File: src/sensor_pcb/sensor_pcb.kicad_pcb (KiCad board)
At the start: 2 copper layers, 34 parts, among them IC1 TCAN3414DRBR, J1 662004231722, J2 643280100305, J3 66200821022, J4 66200821022, J5 662004231722, J6 643280100305, Q2 NPN BJT 40V 200mA, Q3 NPN BJT 40V 200mA, U1 SHT45-AD1B, U2 16-bit ADC, U3 STM32L451CET6, U4 BMP581

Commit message: intermediate changes
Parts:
- removed J6: 643280100305, dz_con:Wuerth_WR_CIRCM_643280100305
- added D1: 150060RS73220, dz_dio:LED_0603, F.Cu at (189.0, 71.0)
- added D10: 150060BS73220, dz_dio:LED_0603, F.Cu at (184.0, 104.0)
- added D11: 150060BS73220, dz_dio:LED_0603, F.Cu at (152.8, 93.0)
- added D12: 150060BS73220, dz_dio:LED_0603, F.Cu at (153.0, 98.7)
- added D13: 150060BS73220, dz_dio:LED_0603, F.Cu at (153.1, 104.9)
- added D4: SMBJ33A, dz_dio:DIOM5436X244N, F.Cu at (142.0, 69.0)
- added D5: 150060GS73220, dz_dio:LED_0603, F.Cu at (172.8, 101.8)
- added D6: SMBJ33A, dz_dio:DIOM5436X244N, F.Cu at (195.0, 69.0)
- added D7: SMBJ33A, dz_dio:DIOM5436X244N, F.Cu at (183.0, 69.0)
- added D8: SMBJ33A, dz_dio:DIOM5436X244N, F.Cu at (154.0, 69.0)
- added D9: 150060RS73220, dz_dio:LED_0603, F.Cu at (148.0, 71.0)
- added J7: 66200421024, dz_con:Wurth_66200421024, F.Cu at (174.0, 64.0)
- added Q1: NPN BJT 40V 200mA, Package_TO_SOT_SMD:SOT-23, F.Cu at (190.9, 104.0)
- added Q4: NPN BJT 40V 200mA, Package_TO_SOT_SMD:SOT-23, F.Cu at (145.8, 93.0)
- added Q5: NPN BJT 40V 200mA, Package_TO_SOT_SMD:SOT-23, F.Cu at (145.9, 99.0)
- added Q6: NPN BJT 40V 200mA, Package_TO_SOT_SMD:SOT-23, F.Cu at (146.0, 105.0)
- added R1: 100, Resistor_SMD:R_0402_1005Metric, F.Cu at (172.8, 99.0)
- added R19: 240, Resistor_SMD:R_0603_1608Metric, F.Cu at (187.1, 103.0)
- added R2: 100, Resistor_SMD:R_0402_1005Metric, F.Cu at (189.5, 69.0)
- added R20: 1k, Resistor_SMD:R_0603_1608Metric, F.Cu at (141.9, 92.0)
- added R21: 27k, Resistor_SMD:R_0603_1608Metric, F.Cu at (141.9, 94.0)
- added R22: 1k, Resistor_SMD:R_0603_1608Metric, F.Cu at (150.0, 92.0)
- added R23: 240, Resistor_SMD:R_0603_1608Metric, F.Cu at (150.0, 94.0)
- added R24: 1k, Resistor_SMD:R_0603_1608Metric, F.Cu at (141.8, 97.9)
- added R25: 27k, Resistor_SMD:R_0603_1608Metric, F.Cu at (141.8, 99.9)
- added R26: 1k, Resistor_SMD:R_0603_1608Metric, F.Cu at (149.8, 97.9)
- added R27: 240, Resistor_SMD:R_0603_1608Metric, F.Cu at (150.0, 99.9)
- added R28: 1k, Resistor_SMD:R_0603_1608Metric, F.Cu at (141.9, 104.0)
- added R29: 27k, Resistor_SMD:R_0603_1608Metric, F.Cu at (141.9, 106.0)
- added R3: 100, Resistor_SMD:R_0402_1005Metric, F.Cu at (148.5, 69.0)
- added R30: 1k, Resistor_SMD:R_0603_1608Metric, F.Cu at (149.9, 104.0)
- added R31: 240, Resistor_SMD:R_0603_1608Metric, F.Cu at (149.9, 106.0)
- added R4: 1k, Resistor_SMD:R_0603_1608Metric, F.Cu at (195.1, 105.0)
- D2, D3: value APHHS1005LSECK/J3-PF -> 150060BS73220; footprint LED_SMD:LED_0402_1005Metric -> dz_dio:LED_0603
- J1: value 662004231722 -> 66200421024; footprint dz_con:Wurth_662004231722 -> dz_con:Wurth_66200421024
- J3: value 66200821022 -> 66200821024; footprint dz_con:Wurth_66200821022 -> dz_con:Wurth_66200821024
- J4: value 66200821022 -> 643280100305; footprint dz_con:Wurth_66200821022 -> dz_con:Wuerth_WR_CIRCM_643280100305
- J5: value 662004231722 -> 66200821024; footprint dz_con:Wurth_662004231722 -> dz_con:Wurth_66200821024
- R7: value 10k -> 27k
- R8: value 10k -> 1k
- moved R7 156.6 mm to (195.1, 103.0), turned to 180 degrees
- moved R10 155.7 mm to (181.2, 76.0), turned to 0 degrees
- moved R11 151.4 mm to (177.2, 76.0), turned to 0 degrees
- moved R8 148.2 mm to (187.1, 105.0), turned to 180 degrees
- moved U2 145.7 mm to (179.0, 80.0)
- moved J1 137.1 mm to (163.0, 64.0), turned to 0 degrees
- moved C2 133.9 mm to (164.0, 106.0), turned to 0 degrees
- moved IC1 114.4 mm to (175.4, 106.0)
- moved C5 114.0 mm to (178.4, 106.0)
- moved R15 90.4 mm to (195.1, 100.0), turned to 180 degrees
- moved R16 89.6 mm to (195.1, 98.0), turned to 180 degrees
- moved U3 86.9 mm to (165.0, 99.8)
- moved R17 85.9 mm to (187.1, 100.0), turned to 180 degrees
- moved D3 84.0 mm to (183.9, 99.0), turned to 90 degrees
- moved Q3 81.5 mm to (190.9, 99.0), turned to 180 degrees
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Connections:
- C1 pad 2: /VDD -> /SCL
- C2 pad 1: /VDD -> /SCL
- C3 pad 1: /VDD -> /SCL
- C4 pad 1: /VDD -> /SCL
- C5 pad 2: /VDD -> /SCL
- IC1 pad 3: /VDD -> /SCL
- J2 pad 3: /VDD -> Net-(J2-Pin_3)
- J3 pad 1: unconnected-(J3-Pad1) -> /ls 4.1
- J3 pad 2: unconnected-(J3-Pad2) -> GND
- J3 pad 3: unconnected-(J3-Pad3) -> /ls 5.1
- J3 pad 4: unconnected-(J3-Pad4) -> GND
- J3 pad 5: unconnected-(J3-Pad5) -> /ls 6.1
- J3 pad 6: unconnected-(J3-Pad6) -> GND
- J4 pad 1: /ls 1.1 -> /CAN_H
- J4 pad 2: GND -> /CAN_L
- J4 pad 3: /ls 2.1 -> Net-(J4-Pin_3)
- J4 pad 4: GND -> /5V
- J4 pad 5: unconnected-(J4-Pad5) -> GND
- J5 pad 1: /VDD -> /ls 1.1
- J5 pad 3: /SDA -> /ls 2.1
- J5 pad 4: /SCL -> GND
- Q2 pad 2: /VDD -> /SCL
- Q3 pad 2: /VDD -> /SCL
- R12 pad 1: /VDD -> /SCL
- R14 pad 2: Net-(D2-A) -> Net-(D2-PadA)
- R16 pad 1: /VDD -> /SCL
- R18 pad 2: Net-(D3-A) -> Net-(D3-PadA)
- R5 pad 2: /VDD -> /SCL
- R6 pad 1: /SDA -> /SCL
- R6 pad 2: /VDD -> /SCL
- R7 pad 1: /VDD -> /SCL
- R7 pad 2: /SCL -> Net-(Q1-B)
- R8 pad 1: /VDD -> /s 3.1
- R8 pad 2: /SDA -> GND
- U1 pad 1: /SDA -> /SCL
- U1 pad 3: /VDD -> /SCL
- U2 pad 8: /VDD -> /SCL
- U2 pad 9: /SDA -> /SCL
- U3 pad 10: /CAN_RX -> /stm/PA0
- U3 pad 14: /SDA -> /SCL
- U3 pad 16: unconnected-(U3-PA6-Pad16) -> /SHDN
- U3 pad 18: /s 2.1 -> /s 1.1
- U3 pad 19: /s 1.1 -> /s 2.1
- U3 pad 20: unconnected-(U3-PB2-Pad20) -> /s 3.1
- U3 pad 24: /VDD -> /SCL
- U3 pad 26: unconnected-(U3-PB13-Pad26) -> /stm/PB13
- U3 pad 30: /SHDN -> /stm/PA9
- U3 pad 39: unconnected-(U3-PB3-Pad39) -> /s 4.1
- U3 pad 40: unconnected-(U3-PB4-Pad40) -> /s 5.1
- U3 pad 41: unconnected-(U3-PB5-Pad41) -> /s 6.1
- U3 pad 42: unconnected-(U3-PB6-Pad42) -> /stm/PB6
- U3 pad 43: unconnected-(U3-PB7-Pad43) -> /stm/PB7
- U4 pad 1: /VDD -> /SCL
- U4 pad 10: /VDD -> /SCL
- U4 pad 4: /SDA -> /SCL
- U4 pad 5: GND -> /SCL
- U4 pad 6: /VDD -> /SCL
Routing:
- net GND: track 499.4 -> 57.2 mm, vias 2 -> 0
- net /VDD: track 350.7 -> 0.00 mm, vias 4 -> 0
- net /SDA: track 201.9 -> 0.00 mm, vias 4 -> 0
- net /SCL: track 179.6 -> 66.2 mm, vias 4 -> 0
- net /s 2.1: track 80.1 -> 31.5 mm, vias 0 -> 2
- net /s 1.1: track 0.00 -> 38.5 mm, vias 0 -> 2
- net /SHDN: track 47.5 -> 15.5 mm
- net /s 4.1: track 0.00 -> 31.1 mm, vias 0 -> 2
- net /s 6.1: track 0.00 -> 31.0 mm, vias 0 -> 2
- net /s 3.1: track 0.00 -> 29.0 mm, vias 0 -> 2
- net /CAN_L: track 41.8 -> 70.8 mm, vias 2 -> 1
- net /ls 6.1: track 0.00 -> 28.8 mm
- net /CAN_H: track 31.2 -> 59.9 mm, vias 0 -> 1
- net /s 5.1: track 0.00 -> 25.9 mm
- net /ls 4.1: track 0.00 -> 23.9 mm
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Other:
- board outline added: 64 x 64 mm

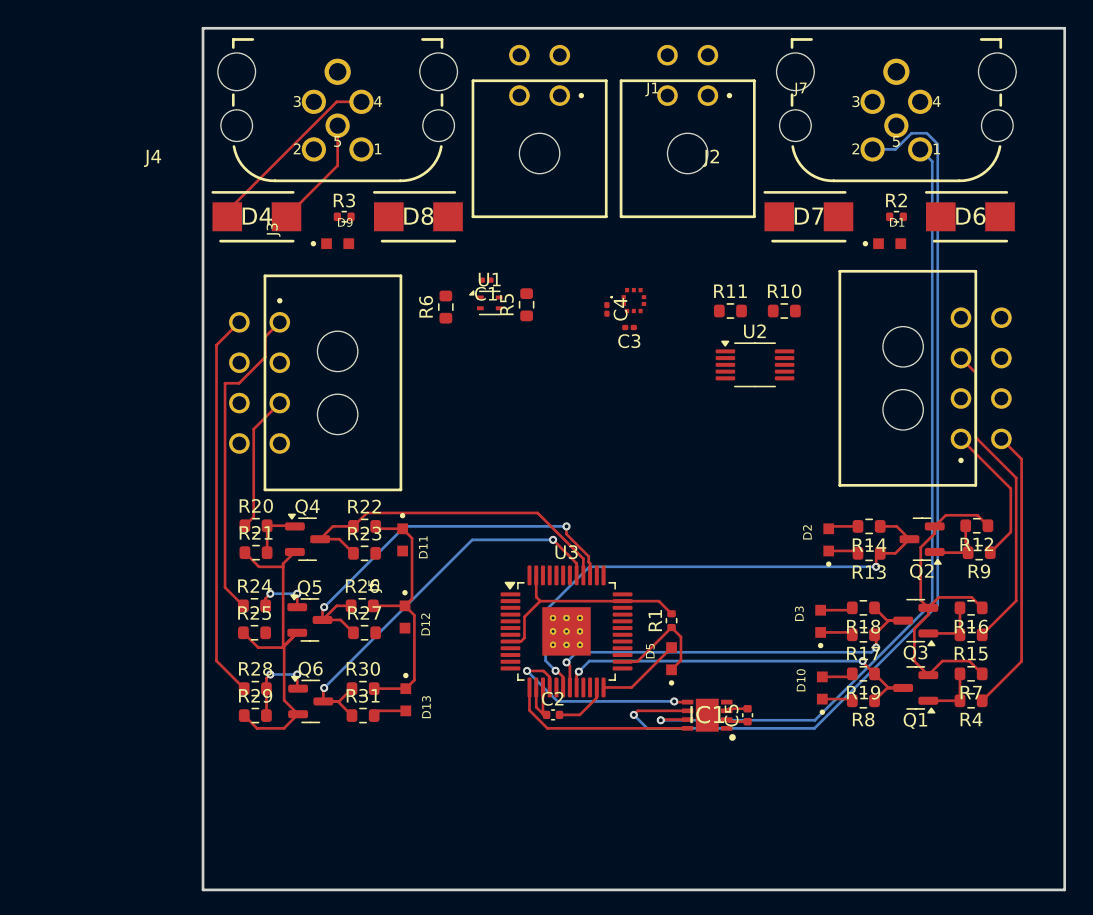
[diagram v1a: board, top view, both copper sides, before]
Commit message: fixing up parts according to kicad auto errors
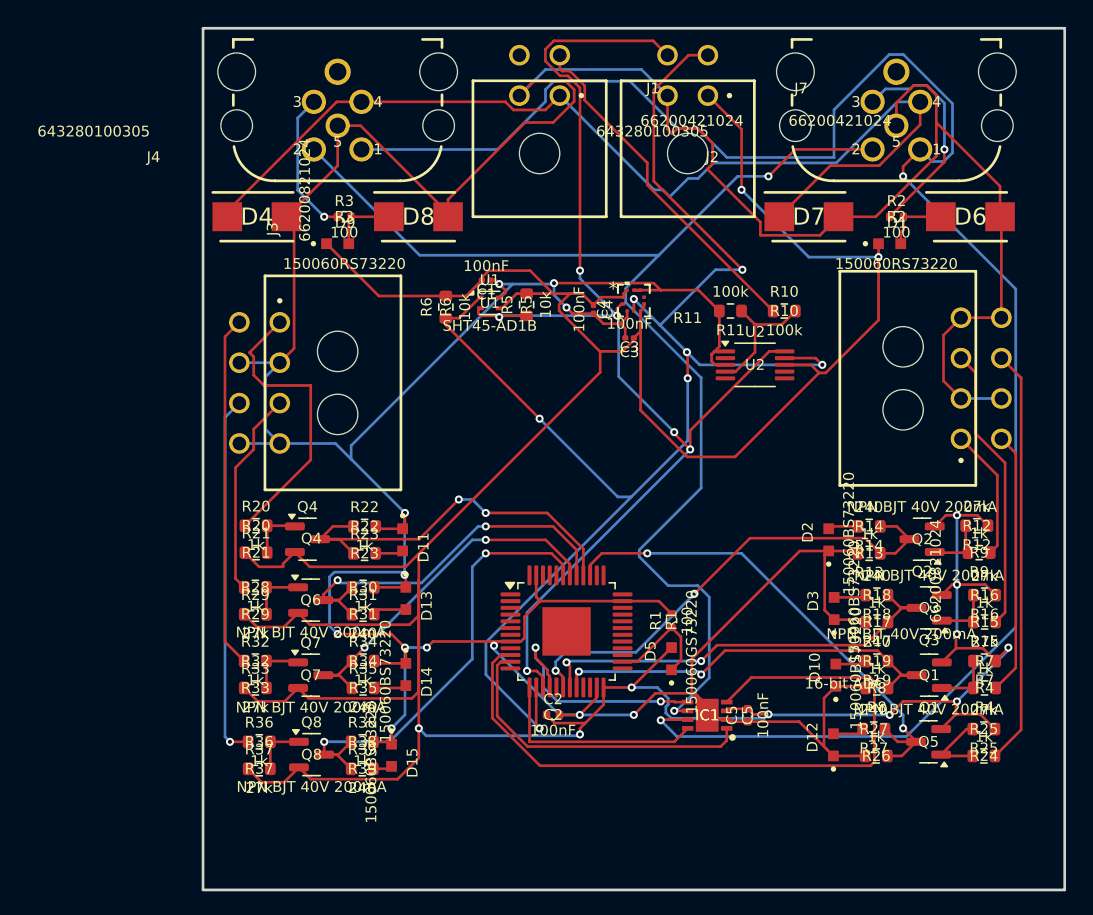
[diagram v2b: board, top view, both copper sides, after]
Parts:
- added D14: 150060BS73220, dz_dio:LED_0603, F.Cu at (153.1, 103.0)
- added D15: 150060BS73220, dz_dio:LED_0603, F.Cu at (152.0, 109.0)
- added Q7: NPN BJT 40V 200mA, Package_TO_SOT_SMD:SOT-23, F.Cu at (146.0, 103.0)
- added Q8: NPN BJT 40V 200mA, Package_TO_SOT_SMD:SOT-23, F.Cu at (146.1, 109.0)
- added R32: 1k, Resistor_SMD:R_0603_1608Metric, F.Cu at (141.9, 102.0)
- added R33: 27k, Resistor_SMD:R_0603_1608Metric, F.Cu at (141.9, 104.0)
- added R34: 1k, Resistor_SMD:R_0603_1608Metric, F.Cu at (149.9, 102.0)
- added R35: 240, Resistor_SMD:R_0603_1608Metric, F.Cu at (149.9, 104.0)
- added R36: 1k, Resistor_SMD:R_0603_1608Metric, F.Cu at (142.2, 108.0)
- added R37: 27k, Resistor_SMD:R_0603_1608Metric, F.Cu at (142.2, 110.0)
- added R38: 1k, Resistor_SMD:R_0603_1608Metric, F.Cu at (149.8, 108.0)
- added R39: 240, Resistor_SMD:R_0603_1608Metric, F.Cu at (149.8, 110.0)
- U3: footprint Package_QFP:LQFP-48-1EP_7x7mm_P0.5mm_EP3.6x3.6mm_ThermalVias -> dz_mcu:STM32L451CET6
- U4: footprint dz_sens:BMP581 -> dz_sens:QFN10_BMP581_BOS
- moved R24 55.3 mm to (196.0, 109.0), turned to 180 degrees
- moved R25 54.6 mm to (196.0, 107.0), turned to 180 degrees
- moved Q5 46.8 mm to (191.9, 108.0), turned to 180 degrees
- moved R26 39.8 mm to (188.0, 109.0), turned to 180 degrees
- moved R27 38.5 mm to (187.8, 107.0), turned to 180 degrees
- moved D12 33.2 mm to (184.8, 108.2), turned to 90 degrees
- moved D13 7.53 mm to (153.1, 97.3)
- moved Q6 7.53 mm to (146.0, 97.5)
- moved R28 7.52 mm to (141.9, 96.5)
- moved R29 7.52 mm to (141.9, 98.5)
- moved R30 7.52 mm to (149.9, 96.5)
- moved R31 7.52 mm to (149.9, 98.5)
- moved D10 1.38 mm to (185.0, 103.0)
- moved D3 1.38 mm to (184.9, 98.1)
- moved Q1 1.38 mm to (191.9, 103.0)
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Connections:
- C1 pad 2: /SCL -> /VDD
- C2 pad 1: /SCL -> /VDD
- C3 pad 1: /SCL -> /VDD
- C4 pad 1: /SCL -> /VDD
- C5 pad 2: /SCL -> /VDD
- D1 pad C: /SCL -> /VDD
- D5 pad A: /SCL -> /VDD
- D9 pad C: /SCL -> /VDD
- IC1 pad 3: /SCL -> /VDD
- J3 pad 1: /ls 4.1 -> /ls 5.1
- J3 pad 3: /ls 5.1 -> /ls 6.1
- J3 pad 5: /ls 6.1 -> /ls 7.1
- J3 pad 7: unconnected-(J3-Pad7) -> /ls 8.1
- J3 pad 8: unconnected-(J3-Pad8) -> GND
- J5 pad 7: unconnected-(J5-Pad7) -> /ls 4.1
- J5 pad 8: unconnected-(J5-Pad8) -> GND
- J7 pad 1: /SCL -> /VDD
- J7 pad 3: /SCL -> /SDA
- Q1 pad 2: /SCL -> /VDD
- Q2 pad 2: /SCL -> /VDD
- Q3 pad 2: /SCL -> /VDD
- Q4 pad 2: /SCL -> /VDD
- Q5 pad 2: /SCL -> /VDD
- Q6 pad 2: /SCL -> /VDD
- R12 pad 1: /SCL -> /VDD
- R16 pad 1: /SCL -> /VDD
- R21 pad 1: /SCL -> /VDD
- R25 pad 1: /SCL -> /VDD
- R29 pad 1: /SCL -> /VDD
- R5 pad 2: /SCL -> /VDD
- R6 pad 1: /SCL -> /SDA
- R6 pad 2: /SCL -> /VDD
- R7 pad 1: /SCL -> /VDD
- U1 pad 1: /SCL -> /SDA
- U1 pad 3: /SCL -> /VDD
- U2 pad 8: /SCL -> /VDD
- U2 pad 9: /SCL -> /SDA
- U3 pad 10: /stm/PA0 -> /CAN_RX
- U3 pad 14: /SCL -> /SDA
- U3 pad 24: /SCL -> /VDD
- U3 pad 42: /stm/PB6 -> /s 7.1
- U3 pad 43: /stm/PB7 -> /s 8.1
- U4 pad 1: /SCL -> /VDD
- U4 pad 10: /SCL -> /VDD
- U4 pad 4: /SCL -> /SDA
- U4 pad 5: /SCL -> /VDD
- U4 pad 6: /SCL -> /VDD
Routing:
- net /VDD: track 0.00 -> 296.6 mm, vias 0 -> 12
- net GND: track 57.2 -> 351.5 mm, vias 0 -> 12
- net /SDA: track 0.00 -> 110.2 mm, vias 0 -> 7
- net /CAN_H: track 59.9 -> 134.0 mm, vias 1 -> 2
- net /5V: track 13.7 -> 77.0 mm
- net /CAN_RX: track 0.00 -> 53.4 mm
- net /s 8.1: track 0.00 -> 34.5 mm, vias 0 -> 2
- net /ls 8.1: track 0.00 -> 27.1 mm, vias 0 -> 1
- net /SCL: track 66.2 -> 92.9 mm, vias 0 -> 6
- net /s 7.1: track 0.00 -> 26.6 mm, vias 0 -> 2
- net /ls 7.1: track 0.00 -> 26.2 mm
- net /p_out: track 0.00 -> 25.9 mm
- net /CAN_TX: track 0.00 -> 23.9 mm
- net /CAN_L: track 70.8 -> 92.7 mm, vias 1 -> 2
- net Net-(J2-Pin_3): track 0.00 -> 16.5 mm, vias 0 -> 1
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
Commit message: removed error messages
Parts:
- D4, D6, D7, D8: value SMBJ33A -> SMBJ3.3A; footprint dz_dio:DIOM5436X244N -> Diode_SMD:D_SMB
- moved D6 12.0 mm to (183.0, 69.0)
- moved D7 12.0 mm to (195.0, 69.0)
- moved D4 0.48 mm to (142.2, 68.6)
- moved J4 0.23 mm to (148.0, 62.0)
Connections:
- D1 pad A: Net-(D6-K) -> Net-(D7-A1)
- D4 pad 1: /5V -> +5V
- D6 pad 1: Net-(D6-K) -> +5V
- D7 pad 1: /5V -> Net-(D7-A1)
- J1 pad 1: /5V -> +5V
- J2 pad 4: /5V -> +5V
- J4 pad 4: /5V -> +5V
- R2 pad 2: Net-(D6-K) -> Net-(D7-A1)
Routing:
- net +5V: track 0.00 -> 77.1 mm
- net /5V: track 77.0 -> 0.00 mm
- net GND: track 351.5 -> 357.6 mm
- net Net-(D7-A1): track 0.00 -> 4.86 mm
- net Net-(D6-K): track 4.86 -> 0.00 mm

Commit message: Sensor PCB suggestion Davide
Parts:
- removed C2: 100nF, Capacitor_SMD:C_0402_1005Metric
- removed D5: 150060GS73220, dz_dio:LED_0603
- removed R1: 100, Resistor_SMD:R_0402_1005Metric
- removed U3: STM32L451CET6, dz_mcu:STM32L451CET6
- moved IC1 19.9 mm to (180.0, 86.6), turned to 90 degrees
- moved C5 16.3 mm to (180.3, 89.8)
- moved J5 6.10 mm to (196.4, 80.8), turned to 90 degrees
- moved J3 3.98 mm to (143.7, 81.5), turned to -90 degrees
- moved J7 3.96 mm to (173.7, 60.0), turned to 180 degrees
- moved J1 3.96 mm to (162.8, 60.0), turned to 180 degrees
- turned R10 to 180 degrees
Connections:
- C1 pad 2: /VDD -> +3.3V
- C3 pad 1: /VDD -> +3.3V
- C4 pad 1: /VDD -> +3.3V
- C5 pad 2: /VDD -> +3.3V
- D1 pad C: /VDD -> +3.3V
- D8 pad 1: Net-(D8-A1) -> +3.3V
- D9 pad A: Net-(D8-A1) -> Net-(D9-PadA)
- D9 pad C: /VDD -> GND
- IC1 pad 3: /VDD -> +3.3V
- J4 pad 3: Net-(J4-Pin_3) -> +3.3V
- J7 pad 1: /VDD -> +3.3V
- Q1 pad 2: /VDD -> +3.3V
- Q2 pad 2: /VDD -> +3.3V
- Q3 pad 2: /VDD -> +3.3V
- Q4 pad 2: /VDD -> +3.3V
- Q5 pad 2: /VDD -> +3.3V
- Q6 pad 2: /VDD -> +3.3V
- Q7 pad 2: /VDD -> +3.3V
- Q8 pad 2: /VDD -> +3.3V
- R12 pad 1: /VDD -> +3.3V
- R16 pad 1: /VDD -> +3.3V
- R21 pad 1: /VDD -> +3.3V
- R25 pad 1: /VDD -> +3.3V
- R29 pad 1: /VDD -> +3.3V
- R3 pad 1: Net-(J4-Pin_3) -> +3.3V
- R3 pad 2: Net-(D8-A1) -> Net-(D9-PadA)
- R33 pad 1: /VDD -> +3.3V
- R37 pad 1: /VDD -> +3.3V
- R5 pad 2: /VDD -> +3.3V
- R6 pad 2: /VDD -> +3.3V
- R7 pad 1: /VDD -> +3.3V
- U1 pad 3: /VDD -> +3.3V
- U2 pad 8: /VDD -> +3.3V
- U4 pad 1: /VDD -> +3.3V
- U4 pad 10: /VDD -> +3.3V
- U4 pad 5: /VDD -> +3.3V
- U4 pad 6: /VDD -> +3.3V
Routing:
- net GND: track 357.6 -> 4.14 mm, vias 12 -> 2
- net /VDD: track 296.6 -> 0.00 mm, vias 12 -> 0
- net /SDA: track 110.2 -> 48.6 mm, vias 7 -> 2
- net /CAN_H: track 134.0 -> 73.0 mm
- net +5V: track 77.1 -> 22.0 mm, vias 0 -> 4
- net +3.3V: track 0.00 -> 54.4 mm, vias 0 -> 29
- net /CAN_RX: track 53.4 -> 0.00 mm
- net /SCL: track 92.9 -> 42.2 mm, vias 6 -> 2
- net /s 4.1: track 37.0 -> 4.77 mm, vias 2 -> 0
- net /s 1.1: track 35.7 -> 4.57 mm, vias 2 -> 0
- net /s 8.1: track 34.5 -> 4.39 mm, vias 2 -> 0
- net /s 2.1: track 32.2 -> 4.52 mm, vias 2 -> 0
- net /s 3.1: track 30.4 -> 4.56 mm, vias 2 -> 0
- net /s 5.1: track 30.0 -> 4.87 mm, vias 2 -> 0
- net /s 6.1: track 29.2 -> 4.52 mm, vias 2 -> 0
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- added copper zone on In2.Cu, net +3.3V
- added copper zone on In2.Cu, net +5V
- added copper zone on F.Cu, net GND
- added copper zone on In1.Cu, net GND
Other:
- copper layers 2 -> 4

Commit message: clearing up errors
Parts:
- added C10: 100nF, Capacitor_SMD:C_0603_1608Metric, F.Cu at (150.3, 143.6)
- added C11: 100nF, Capacitor_SMD:C_0603_1608Metric, F.Cu at (150.3, 140.2)
- added C12: 4.7uF, Capacitor_SMD:C_0402_1005Metric, F.Cu at (174.0, 140.5)
- added C2: 100nF, Capacitor_SMD:C_0402_1005Metric, F.Cu at (157.1, 116.0)
- added C26: 10pF, Capacitor_SMD:C_0603_1608Metric, F.Cu at (165.4, 114.7)
- added C31: 10pF, Capacitor_SMD:C_0603_1608Metric, F.Cu at (165.4, 117.2)
- added C6: 100nF, Capacitor_SMD:C_0603_1608Metric, F.Cu at (163.9, 140.0)
- added C7: 10nF, Capacitor_SMD:C_0603_1608Metric, F.Cu at (159.6, 149.4)
- added C8: 100nF, Capacitor_SMD:C_0603_1608Metric, F.Cu at (153.4, 154.6)
- added C9: 1uF, Capacitor_SMD:C_0603_1608Metric, F.Cu at (154.7, 135.9)
- added FB2: 100Ω@100MHz, Inductor_SMD:L_0603_1608Metric, F.Cu at (179.5, 145.6)
- added J6: FTSH-107-02-L-DV, dz_con:FTSH-107-XX-YYY-DV, F.Cu at (176.1, 104.5)
- added R1: 10k, Resistor_SMD:R_0603_1608Metric, F.Cu at (165.4, 154.0)
- added R40: 0, Resistor_SMD:R_0201_0603Metric, F.Cu at (167.1, 146.1)
- added SW1: Button Switch SPST-No, Button_Switch_THT:SW_PUSH_6mm, F.Cu at (171.6, 151.4)
- added U3: STM32L451CET6, dz_mcu:STM32L451CET6, F.Cu at (157.1, 142.6)
- added Y1: 16.0MHz, Crystal:Crystal_SMD_3225-4Pin_3.2x2.5mm, F.Cu at (180.6, 113.2)
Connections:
- net /SCL renamed /sensor_stm/SCL
- net /SDA renamed /sensor_stm/SDA

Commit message: final changes before review
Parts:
- removed C12: 4.7uF, Capacitor_SMD:C_0402_1005Metric
- removed R40: 0, Resistor_SMD:R_0201_0603Metric
- added C13: 100nF, Capacitor_SMD:C_0603_1608Metric, F.Cu at (169.1, 94.0)
- added C14: 100nF, Capacitor_SMD:C_0603_1608Metric, F.Cu at (163.8, 80.6)
- added C15: 4.7nF, Capacitor_SMD:C_0603_1608Metric, F.Cu at (172.1, 83.2)
- added R41: 0, Resistor_SMD:R_0603_1608Metric, F.Cu at (174.3, 87.2)
- moved C8 67.7 mm to (159.8, 87.2), turned to 180 degrees
- moved R1 66.5 mm to (157.4, 88.0)
- moved FB2 58.8 mm to (172.6, 87.2), turned to 90 degrees
- moved C9 56.3 mm to (165.4, 80.6)
- moved C6 56.1 mm to (173.4, 84.8)
- moved U3 56.1 mm to (166.6, 87.3)
- moved C11 56.1 mm to (159.8, 84.9)
- moved C7 55.9 mm to (167.5, 94.1)
- moved C10 55.6 mm to (159.8, 88.8)
- moved SW1 52.1 mm to (163.4, 99.9), turned to 180 degrees
- moved C2 44.4 mm to (183.4, 80.2)
- moved Y1 38.3 mm to (155.8, 84.0), turned to 180 degrees
- moved C31 37.4 mm to (155.3, 81.3), turned to 180 degrees
- moved C26 36.7 mm to (155.2, 79.5), turned to 180 degrees
- moved J6 8.81 mm to (176.9, 95.8)
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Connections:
- C5 pad 1: GND -> +3.3V
- C5 pad 2: +3.3V -> GND
- C8 pad 1: Net-(U3-NRST) -> /sensor_stm/nRST
- IC1 pad 1: /CAN_TX -> /sensor_stm/CAN.TX
- IC1 pad 4: /CAN_RX -> /sensor_stm/CAN.RX
- IC1 pad 8: /STB -> GND
- R1 pad 2: Net-(U3-NRST) -> /sensor_stm/nRST
- SW1 pad 2: Net-(U3-NRST) -> /sensor_stm/nRST
- U3 pad 25: /sensor_stm/CAN.TX -> /sensor_stm/CAN.RX
- U3 pad 7: Net-(U3-NRST) -> /sensor_stm/nRST
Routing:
- net /sensor_stm/nRST: track 0.00 -> 43.2 mm, vias 0 -> 3
- net +3.3V: track 54.4 -> 90.2 mm, vias 29 -> 37
- net GND: track 4.14 -> 39.6 mm, vias 2 -> 21
- net /sensor_stm/UART0.RX: track 0.00 -> 27.4 mm, vias 0 -> 2
- net /sensor_stm/UART0.TX: track 0.00 -> 25.7 mm, vias 0 -> 2
- net /sensor_stm/JTAG_TDI: track 0.00 -> 21.7 mm, vias 0 -> 2
- net /sensor_stm/JTAG_TDO/SWD: track 0.00 -> 17.5 mm, vias 0 -> 2
- net /sensor_stm/OSC_OUT: track 0.00 -> 15.2 mm, vias 0 -> 2
- net /sensor_stm/OSC_IN: track 0.00 -> 15.1 mm, vias 0 -> 2
- net /sensor_stm/JTAG_TCK/SWCLK: track 0.00 -> 15.1 mm, vias 0 -> 2
- net +5V: track 22.0 -> 7.76 mm
- net /sensor_stm/CAN.RX: track 0.00 -> 13.2 mm, vias 0 -> 2
- net /sensor_stm/JTAG_TMS/SWDIO: track 0.00 -> 11.6 mm, vias 0 -> 2
- net /CAN_L: track 87.3 -> 76.6 mm, vias 3 -> 1
- net /sensor_stm/CAN.TX: track 0.00 -> 8.89 mm
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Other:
- board size 64 x 64 mm -> 64 x 58.4 mm
